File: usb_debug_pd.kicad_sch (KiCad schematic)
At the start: 85 parts, among them J4 Tag-Connect_TC2050-IDC-NL_2x5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, J7 USB-C_Kycon_KUSBX-SL2-CS1N24-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, Q12 PJE138K, Q3 PJE138K, U29 W25Q80DV_USON, U30 TPS65988DHRSHR, U31 NTS0102_XSON, U32 NCP730BMT330_WSON, U34 FT230X_QFN, U40 AP22615A_TSOT26, U42 TPD4E05U06QDQARQ1

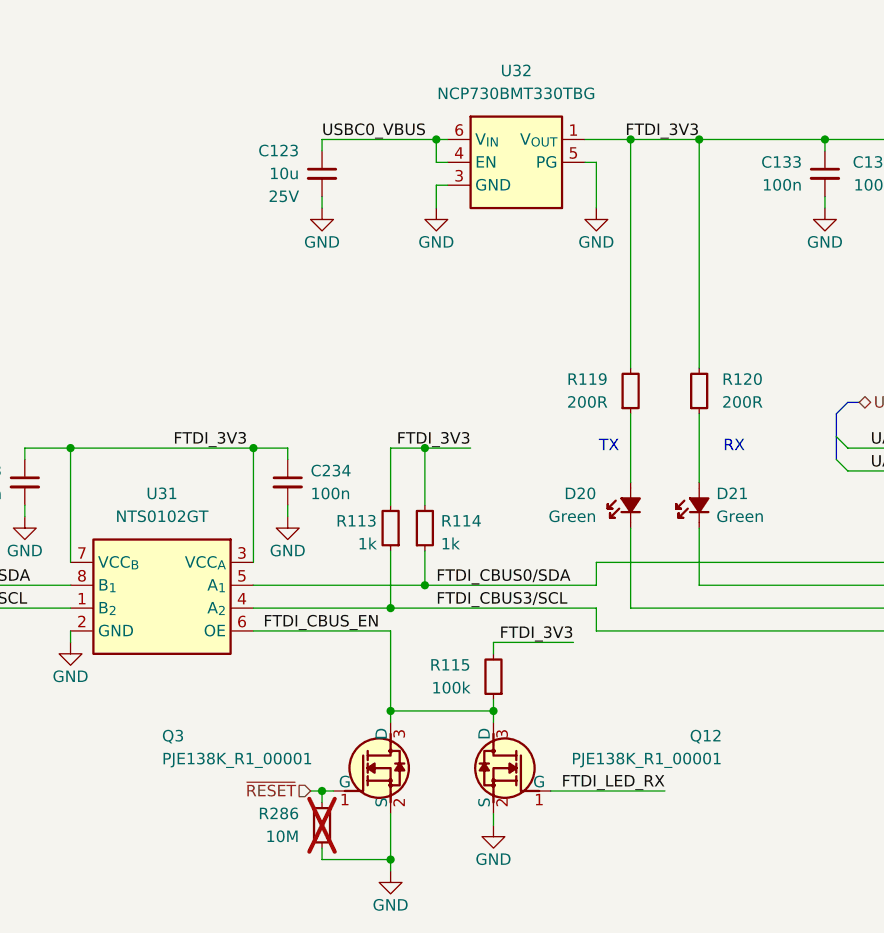
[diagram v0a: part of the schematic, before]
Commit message: [#85326] Add reviewers suggestions; Unify BOM
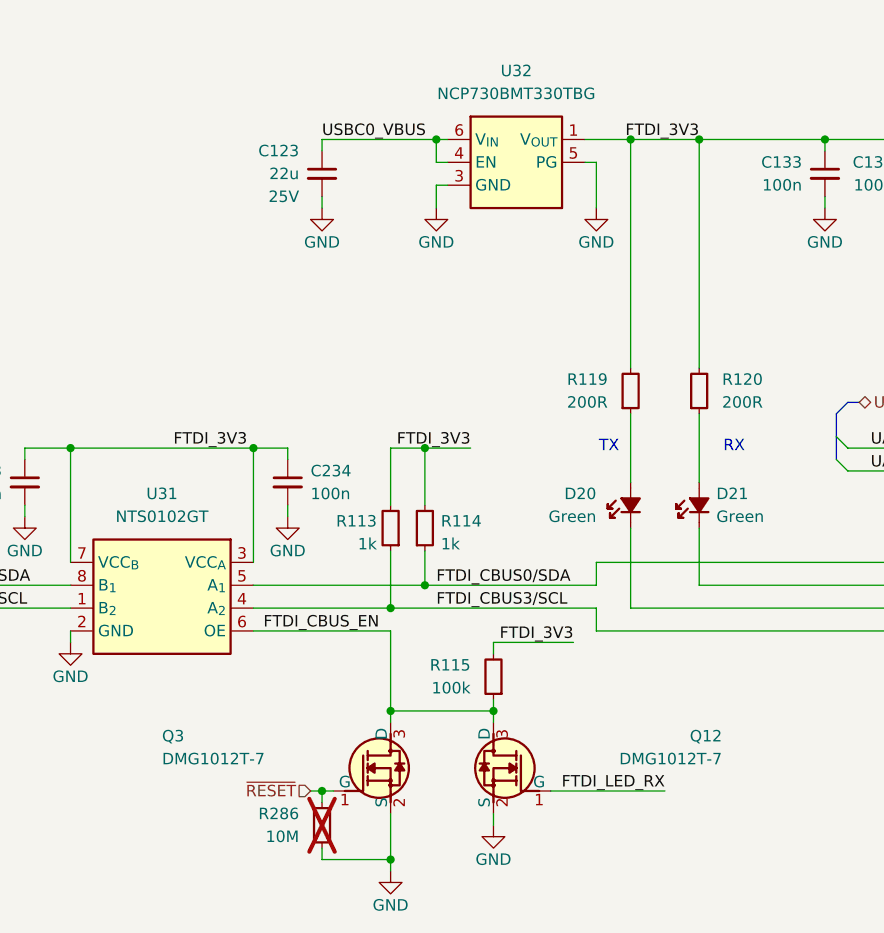
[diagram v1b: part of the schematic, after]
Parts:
- C123: value C_10u_25V_0603 -> C_22u_25V_0805; footprint antmicro-footprints:C_0603_1608Metric -> antmicro-footprints:C_0805_2012Metric; symbol antmicroCapacitors0603:C_10u_25V_0603 -> antmicroCapacitorsmisc:C_22u_25V_0805; Dielectric (none) -> X5R; MPN C1608X5R1E106M080AC -> CL21A226MAYNNNE; Manufacturer TDK -> Samsung Electro-Mechanics; Public (none) -> False; Val 10u -> 22u
- Q12, Q3: value PJE138K -> DMG1012T-7; symbol antmicroTransistorsFETsMOSFETsSingle:PJE138K -> antmicroTransistorsFETsMOSFETsSingle:DMG1012T-7; MPN PJE138K_R1_00001 -> DMG1012T-7; Manufacturer PANJIT -> Diodes Incorporated
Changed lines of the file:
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@@
 	)
 	(symbol
-		(lib_id "antmicroCapacitors0603:C_10u_25V_0603")
+		(lib_id "antmicroCapacitorsmisc:C_22u_25V_0805")
 		(at 78.74 66.04 90)
 		(mirror x)
@@
 			)
 		)
-		(property "Value" "C_10u_25V_0603"
+		(property "Value" "C_22u_25V_0805"
 			(at 88.9 86.36 0)
 			(effects
@@
 			)
 		)
-		(property "Footprint" "antmicro-footprints:C_0603_1608Metric"
+		(property "Footprint" "antmicro-footprints:C_0805_2012Metric"
 			(at 91.44 86.36 0)
 			(effects
@@
 			)
 		)
-		(property "Datasheet" "https://product.tdk.com/en/search/capacitor/ceramic/mlcc/info?part_no=C1608X5R1E106M080AC"
+		(property "Datasheet" "https://product.samsungsem.com/mlcc/CL21A226MAYNNN.do"
 			(at 93.98 86.36 0)
 			(effects
@@
 			)
 		)
-		(property "Description" "SMD Multilayer Ceramic Capacitor, 10 µF, 25 V, 0603 [1608 Metric], ± 20%, X5R, C"
+		(property "Description" "SMT Multilayer Ceramic Capacitor, 22uF, +/-20%, 25V, X5R, 0805 [2012 Metric]"
 			(at 78.74 66.04 0)
 			(effects
@@
 			)
 		)
-		(property "Manufacturer" "TDK"
+		(property "Manufacturer" "Samsung Electro-Mechanics"
 			(at 99.06 86.36 0)
 			(effects
@@
 			)
 		)
-		(property "MPN" "C1608X5R1E106M080AC"
+		(property "MPN" "CL21A226MAYNNNE"
 			(at 96.52 86.36 0)
 			(effects
@@
 			)
 		)
-		(property "Val" "10u"
+		(property "Val" "22u"
 			(at 76.2 68.5863 90)
 			(effects
@@
 			)
 		)
-		(property "Dielectric" ""
+		(property "Dielectric" "X5R"
 			(at 109.22 86.36 0)
+			(effects
+				(font
+					(size 1.27 1.27)
+				)
+				(justify left bottom)
+				(hide yes)
+			)
+		)
+		(property "Public" "False"
+			(at 111.76 86.36 0)
 			(effects
 				(font
@@
 	)
 	(symbol
-		(lib_id "antmicroTransistorsFETsMOSFETsSingle:PJE138K")
+		(lib_id "antmicroTransistorsFETsMOSFETsSingle:DMG1012T-7")
 		(at 80.01 137.16 0)
 		(unit 1)
@@
 			)
 		)
-		(property "Value" "PJE138K"
+		(property "Value" "DMG1012T-7"
 			(at 102.87 146.05 0)
 			(effects
@@
 			)
 		)
-		(property "Datasheet" "https://www.mouser.com/datasheet/2/1057/PJE138K-1876698.pdf"
+		(property "Datasheet" "https://www.diodes.com/assets/Datasheets/ds31783.pdf"
 			(at 102.87 151.13 0)
 			(effects
@@
 			)
 		)
-		(property "Description" "MOSFET, N Channel, 50V, 0.35A, 4.5 ohm, SOT-523, Surface Mount"
+		(property "Description" "Power MOSFET, N Channel, 20 V, 630 mA, 0.3 ohm, SOT-523, Surface Mount"
 			(at 102.87 163.83 0)
 			(effects
@@
 			)
 		)
-		(property "MPN" "PJE138K_R1_00001"
+		(property "MPN" "DMG1012T-7"
 			(at 60.96 133.604 0)
 			(effects
@@
 			)
 		)
-		(property "Manufacturer" "PANJIT"
+		(property "Manufacturer" "Diodes Incorporated"
 			(at 102.87 156.21 0)
 			(effects
@@
 	)
 	(symbol
-		(lib_id "antmicroTransistorsFETsMOSFETsSingle:PJE138K")
+		(lib_id "antmicroTransistorsFETsMOSFETsSingle:DMG1012T-7")
 		(at 104.14 137.16 0)
 		(mirror y)
@@
 			)
 		)
-		(property "Value" "PJE138K"
+		(property "Value" "DMG1012T-7"
 			(at 81.28 146.05 0)
 			(effects
@@
 			)
 		)
-		(property "Datasheet" "https://www.mouser.com/datasheet/2/1057/PJE138K-1876698.pdf"
+		(property "Datasheet" "https://www.diodes.com/assets/Datasheets/ds31783.pdf"
 			(at 81.28 151.13 0)
 			(effects
@@
 			)
 		)
-		(property "Description" "MOSFET, N Channel, 50V, 0.35A, 4.5 ohm, SOT-523, Surface Mount"
+		(property "Description" "Power MOSFET, N Channel, 20 V, 630 mA, 0.3 ohm, SOT-523, Surface Mount"
 			(at 81.28 163.83 0)
 			(effects
@@
 			)
 		)
-		(property "MPN" "PJE138K_R1_00001"
+		(property "MPN" "DMG1012T-7"
 			(at 123.19 133.604 0)
 			(effects
@@
 			)
 		)
-		(property "Manufacturer" "PANJIT"
+		(property "Manufacturer" "Diodes Incorporated"
 			(at 81.28 156.21 0)
 			(effects

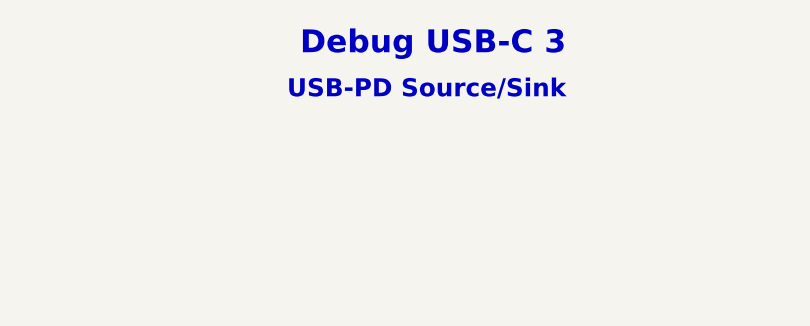
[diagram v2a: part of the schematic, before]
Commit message: [#85326] Update USB naming convention
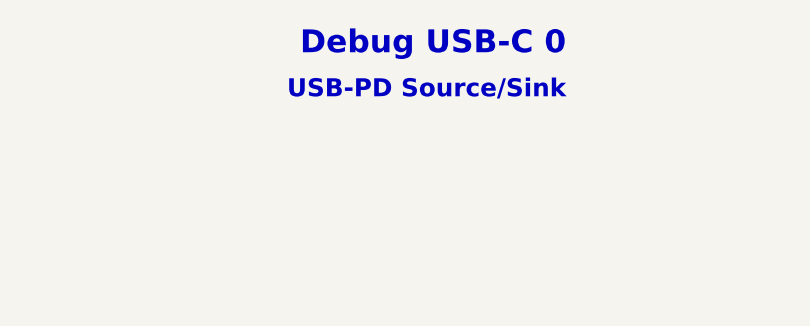
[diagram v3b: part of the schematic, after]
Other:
- note added: "Debug USB-C 0"
- note removed: "Debug USB-C 3"
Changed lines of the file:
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@@
 		(comment 1 "www.antmicro.com")
 	)
-	(text "Debug USB-C 3"
+	(text "Debug USB-C 0"
 		(exclude_from_sim no)
 		(at 213.614 23.114 0)

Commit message: [#85488] After rebase cleanup
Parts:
- U32: value NCP730BMT330_WSON -> NCP718BSN330T1G; footprint antmicro-footprints:WSON-6-1EP_2x2mm_P0.65mm -> antmicro-footprints:SOT-23-5; symbol antmicroPMICVoltageRegulatorsLinear:NCP730BMT330_WSON -> antmicroPMICVoltageRegulatorsLinear:NCP718BSN330T1G; MPN NCP730BMT330TBG -> NCP718BSN330T1G
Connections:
- net FTDI_3V3: now also U32.5 (VOUT); no longer U32.1 (V_{OUT})
- net GND: now also U32.2 (GND); no longer U32.3 (GND), U32.5 (PG), U32.7 (GND)
- net USBC0_VBUS: now also U32.1 (VIN), U32.3 (EN); no longer U32.4 (EN), U32.6 (V_{IN})
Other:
- moved on the sheet: C123

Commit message: [#85326] Clean DRC
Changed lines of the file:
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@@
 	(wire
 		(pts
+			(xy 134.62 63.5) (xy 134.62 64.77)
+		)
+		(stroke
+			(width 0)
+			(type default)
+		)
+	)
+	(wire
+		(pts
 			(xy 149.86 207.01) (xy 158.75 207.01)
 		)
@@
 					(unit 1)
 				)
+			)
+		)
+	)
+	(symbol
+		(lib_id "antmicropower:PWR_FLAG")
+		(at 134.62 63.5 0)
+		(unit 1)
+		(exclude_from_sim no)
+		(in_bom yes)
+		(on_board yes)
+		(dnp no)
+		(property "Reference" "#FLG014"
+			(at 134.62 61.595 0)
+			(effects
+				(font
+					(size 1.27 1.27)
+				)
+				(hide yes)
+			)
+		)
+		(property "Value" "PWR_FLAG"
+			(at 134.62 59.69 0)
+			(effects
+				(font
+					(size 1.27 1.27)
+				)
+			)
+		)
+		(property "Footprint" ""
+			(at 134.62 63.5 0)
+			(effects
+				(font
+					(size 1.27 1.27)
+				)
+				(hide yes)
+			)
+		)
+		(property "Datasheet" ""
+			(at 134.62 63.5 0)
+			(effects
+				(font
+					(size 1.27 1.27)
+				)
+				(hide yes)
+			)
+		)
+		(property "Description" ""
+			(at 134.62 63.5 0)
+			(effects
+				(font
+					(size 1.27 1.27)
+				)
+				(hide yes)
+			)
+		)
+		(pin "1"
+		)
+		(instances
+			(project "jetson-agx-thor-baseboard"
+				(path "/f569b0be-0afd-48b7-93ee-28582a4c645c/12c19ba5-8fdc-4775-a33b-e8b1ade01b0a"
+					(reference "#FLG014")
+					(unit 1)
+				)

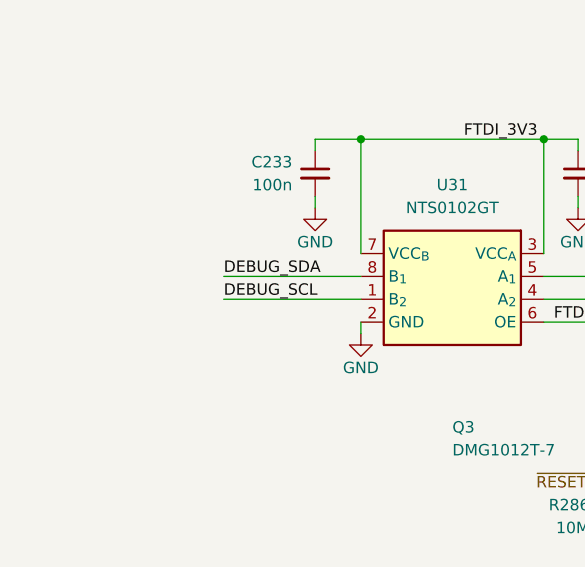
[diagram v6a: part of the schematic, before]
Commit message: [#85326] Add SoM capacitors, add testpoints
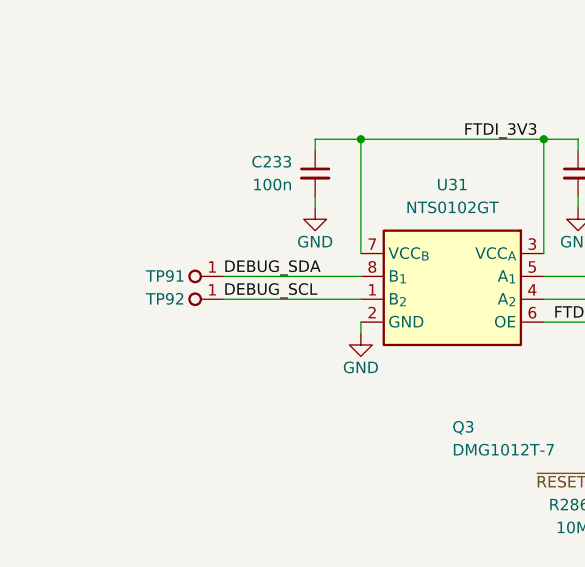
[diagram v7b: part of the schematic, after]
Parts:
- added TP91, TP92: TP_0.75mm_SMD, antmicro-footprints:TP_SMD_0.75mm, symbol antmicroTestPoints:TP_0.75mm_SMD
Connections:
- net DEBUG_SCL: now also TP92.1
- net DEBUG_SDA: now also TP91.1
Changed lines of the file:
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@@
 	)
 	(symbol
+		(lib_id "antmicroTestPoints:TP_0.75mm_SMD")
+		(at 35.56 114.3 180)
+		(unit 1)
+		(exclude_from_sim no)
+		(in_bom no)
+		(on_board yes)
+		(dnp no)
+		(property "Reference" "TP91"
+			(at 31.242 114.3 0)
+			(effects
+				(font
+					(size 1.27 1.27)
+					(thickness 0.15)
+				)
+				(justify left)
+			)
+		)
+		(property "Value" "TP_0.75mm_SMD"
+			(at 25.4 110.49 0)
+			(effects
+				(font
+					(size 1.27 1.27)
+					(thickness 0.15)
+				)
+				(justify left bottom)
+				(hide yes)
+			)
+		)
+		(property "Footprint" "antmicro-footprints:TP_SMD_0.75mm"
+			(at 25.4 107.95 0)
+			(effects
+				(font
+					(size 1.27 1.27)
+					(thickness 0.15)
+				)
+				(justify left bottom)
+				(hide yes)
+			)
+		)
+		(property "Datasheet" ""
+			(at 17.78 101.6 0)
+			(effects
+				(font
+					(size 1.27 1.27)
+					(thickness 0.15)
+				)
+				(justify left bottom)
+				(hide yes)
+			)
+		)
+		(property "Description" "SMT test point"
+			(at 35.56 114.3 0)
+			(effects
+				(font
+					(size 1.27 1.27)
+				)
+				(hide yes)
+			)
+		)
+		(property "MPN" ""
+			(at 24.765 102.87 0)
+			(effects
+				(font
+					(size 1.27 1.27)
+					(thickness 0.15)
+				)
+				(justify left bottom)
+				(hide yes)
+			)
+		)
+		(property "Manufacturer" ""
+			(at 24.765 107.95 0)
+			(effects
+				(font
+					(size 1.27 1.27)
+					(thickness 0.15)
+				)
+				(justify left bottom)
+				(hide yes)
+			)
+		)
+		(property "Author" "Antmicro"
+			(at 25.4 105.41 0)
+			(effects
+				(font
+					(size 1.27 1.27)
+					(thickness 0.15)
+				)
+				(justify left bottom)
+				(hide yes)
+			)
+		)
+		(property "License" "Apache-2.0"
+			(at 25.4 102.87 0)
+			(effects
+				(font
+					(size 1.27 1.27)
+					(thickness 0.15)
+				)
+				(justify left bottom)
+				(hide yes)
+			)
+		)
+		(pin "1"
+		)
+		(instances
+			(project "jetson-agx-thor-baseboard"
+				(path "/f569b0be-0afd-48b7-93ee-28582a4c645c/12c19ba5-8fdc-4775-a33b-e8b1ade01b0a"
+					(reference "TP91")
+					(unit 1)
+				)
+			)
+		)
+	)
+	(symbol
 		(lib_id "antmicroResistors0402:R_1k_0402")
 		(at 90.17 110.49 90)
@@
 					(unit 1)
 				)
+			)
+		)
+	)
+	(symbol
+		(lib_id "antmicroTestPoints:TP_0.75mm_SMD")
+		(at 35.56 116.84 180)
+		(unit 1)
+		(exclude_from_sim no)
+		(in_bom no)
+		(on_board yes)
+		(dnp no)
+		(property "Reference" "TP92"
+			(at 31.242 116.84 0)
+			(effects
+				(font
+					(size 1.27 1.27)
+					(thickness 0.15)
+				)
+				(justify left)
+			)
+		)
+		(property "Value" "TP_0.75mm_SMD"
+			(at 25.4 113.03 0)
+			(effects
+				(font
+					(size 1.27 1.27)
+					(thickness 0.15)
+				)
+				(justify left bottom)
+				(hide yes)
+			)
+		)
+		(property "Footprint" "antmicro-footprints:TP_SMD_0.75mm"
+			(at 25.4 110.49 0)
+			(effects
+				(font
+					(size 1.27 1.27)
+					(thickness 0.15)
+				)
+				(justify left bottom)
+				(hide yes)
+			)
+		)
+		(property "Datasheet" ""
+			(at 17.78 104.14 0)
+			(effects
+				(font
+					(size 1.27 1.27)
+					(thickness 0.15)
+				)
+				(justify left bottom)
+				(hide yes)
+			)
+		)
+		(property "Description" "SMT test point"
+			(at 35.56 116.84 0)
+			(effects
+				(font
+					(size 1.27 1.27)
+				)
+				(hide yes)
+			)
+		)
+		(property "MPN" ""
+			(at 24.765 105.41 0)
+			(effects
+				(font
+					(size 1.27 1.27)
+					(thickness 0.15)
+				)
+				(justify left bottom)
+				(hide yes)
+			)
+		)
+		(property "Manufacturer" ""
+			(at 24.765 110.49 0)
+			(effects
+				(font
+					(size 1.27 1.27)
+					(thickness 0.15)
+				)
+				(justify left bottom)
+				(hide yes)
+			)
+		)
+		(property "Author" "Antmicro"
+			(at 25.4 107.95 0)
+			(effects
+				(font
+					(size 1.27 1.27)
+					(thickness 0.15)
+				)
+				(justify left bottom)
+				(hide yes)
+			)
+		)
+		(property "License" "Apache-2.0"
+			(at 25.4 105.41 0)
+			(effects
+				(font
+					(size 1.27 1.27)
+					(thickness 0.15)
+				)
+				(justify left bottom)
+				(hide yes)
+			)
+		)
+		(pin "1"
+		)
+		(instances
+			(project "jetson-agx-thor-baseboard"
+				(path "/f569b0be-0afd-48b7-93ee-28582a4c645c/12c19ba5-8fdc-4775-a33b-e8b1ade01b0a"
+					(reference "TP92")
+					(unit 1)
+				)
